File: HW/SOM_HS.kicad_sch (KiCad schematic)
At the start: 1 part

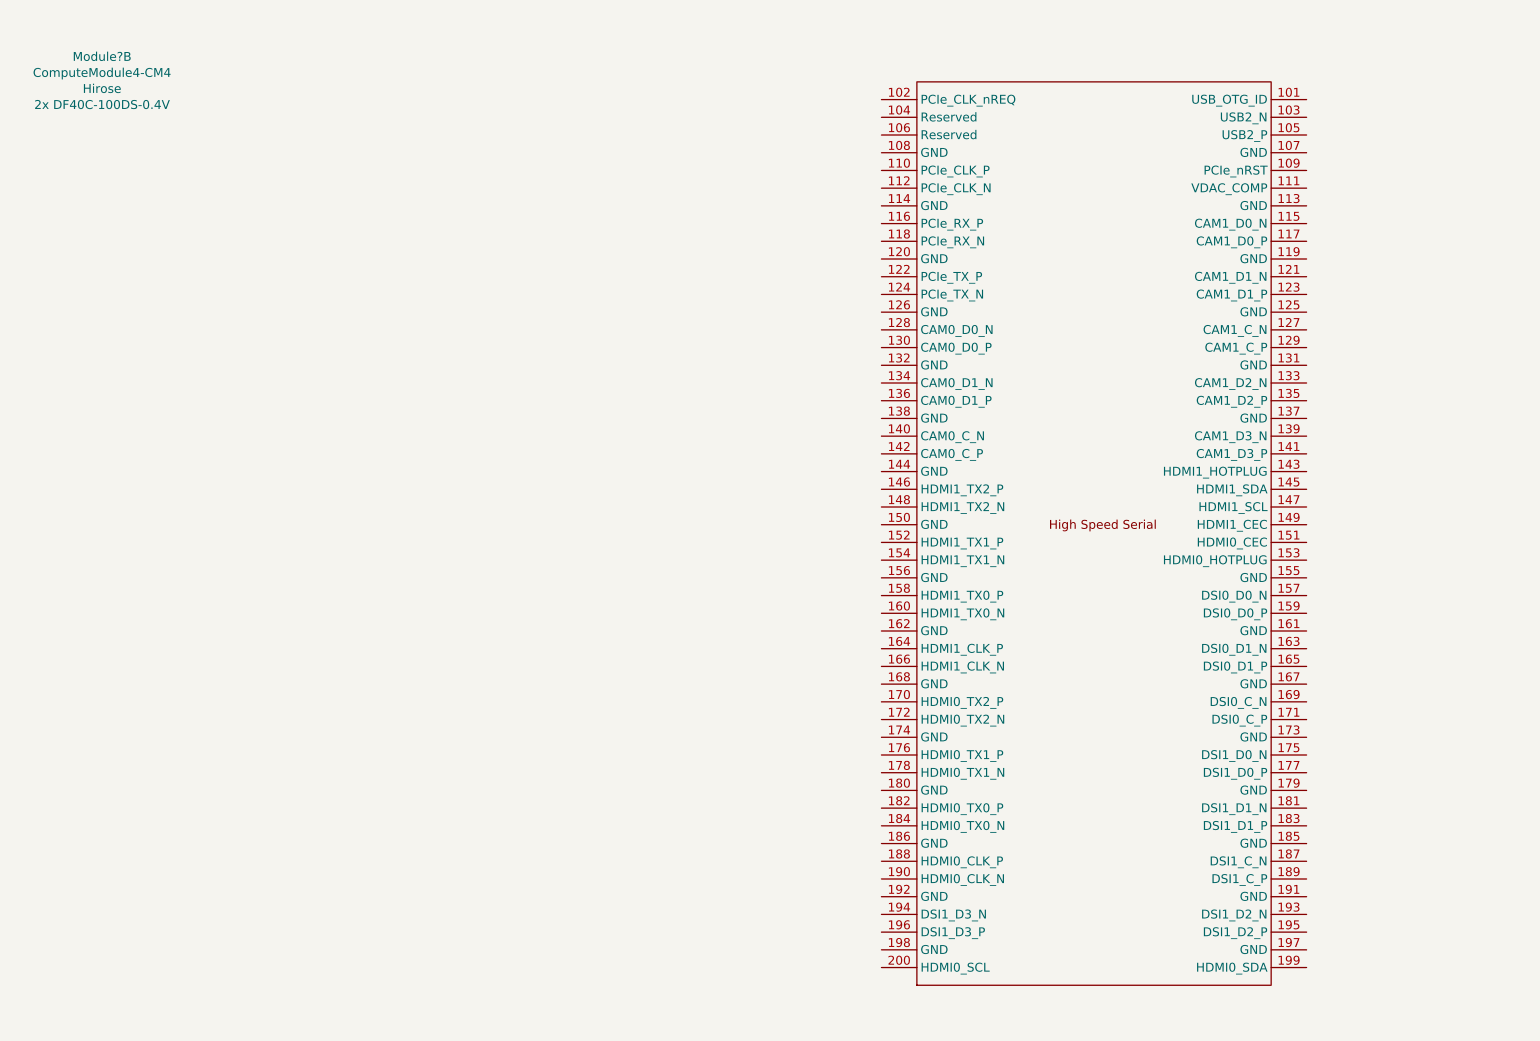
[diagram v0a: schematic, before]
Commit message: added gnds, some connector breakout
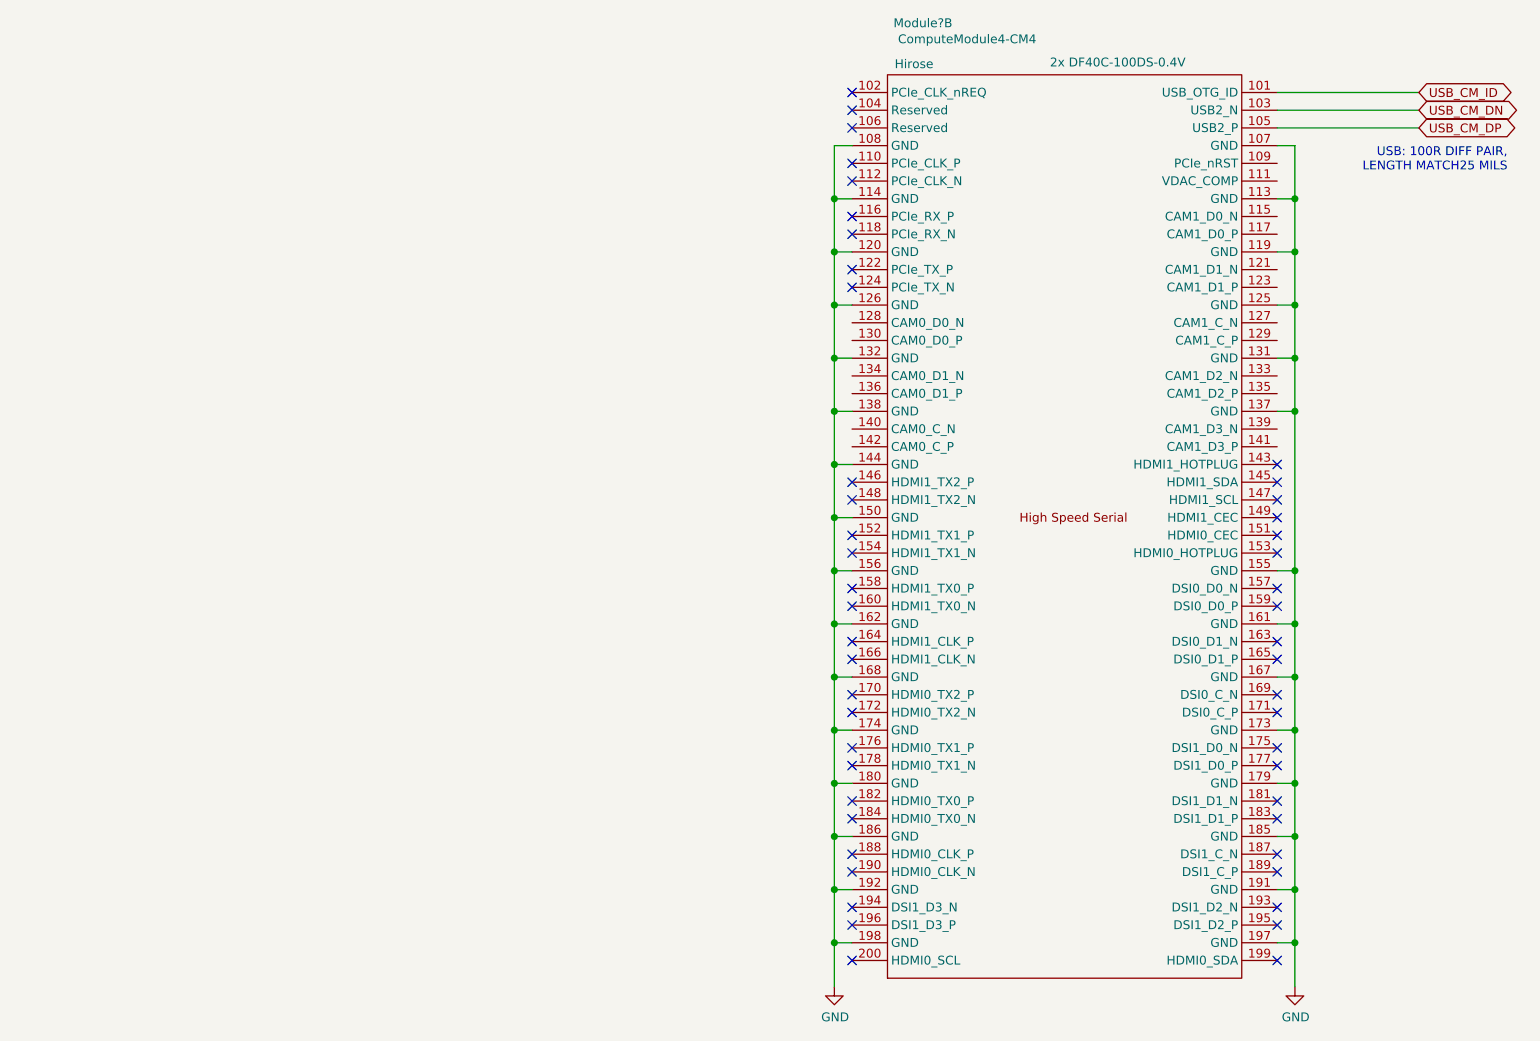
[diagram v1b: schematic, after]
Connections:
- net USB_CM_ID: now reaches Module?.101 (USB_OTG_ID)
- net USB_CM_DN: now reaches Module?.103 (USB2_N)
- net USB_CM_DP: now reaches Module?.105 (USB2_P)
- net GND: now reaches Module?.107 (GND)
- net GND: now also Module?.108 (GND), Module?.113 (GND), Module?.114 (GND), Module?.119 (GND), Module?.120 (GND), Module?.125 (GND), Module?.126 (GND), Module?.131 (GND), Module?.132 (GND), Module?.137 (GND), Module?.138 (GND), Module?.144 (GND), Module?.150 (GND), Module?.155 (GND), Module?.156 (GND), Module?.161 (GND), Module?.162 (GND), Module?.167 (GND), Module?.168 (GND), Module?.173 (GND), Module?.174 (GND), Module?.179 (GND), Module?.180 (GND), Module?.185 (GND), Module?.186 (GND), Module?.191 (GND), Module?.192 (GND), Module?.197 (GND), Module?.198 (GND)
- no-connect marks 0 -> 49
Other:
- note added: "USB: 100R DIFF PAIR, LENGTH MATCH25 MILS"
- moved on the sheet: Module?B
